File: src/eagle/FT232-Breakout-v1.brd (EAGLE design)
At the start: 37.8 x 38.1 mm, 19 parts, among them T1 BC547, U1 FT232RL-BASICSSOP

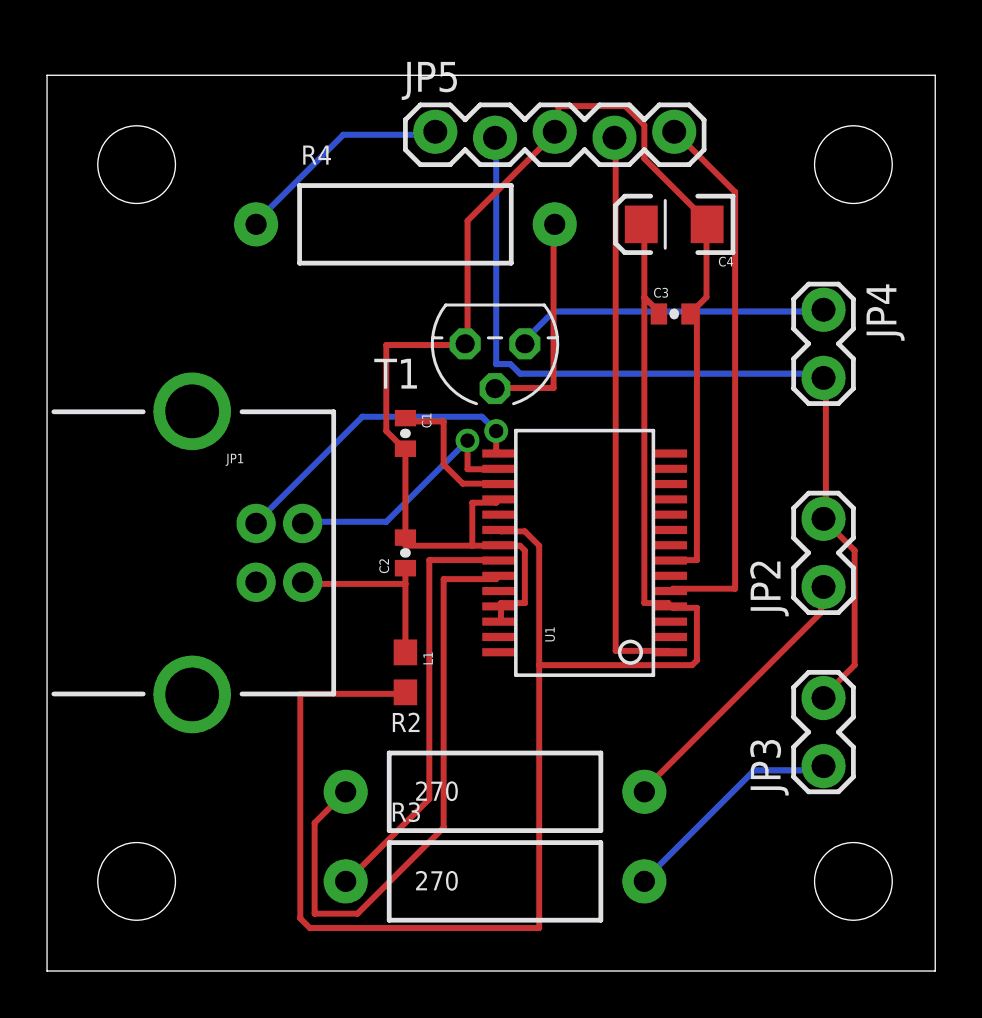
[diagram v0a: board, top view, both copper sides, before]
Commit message: modified daughter board for production
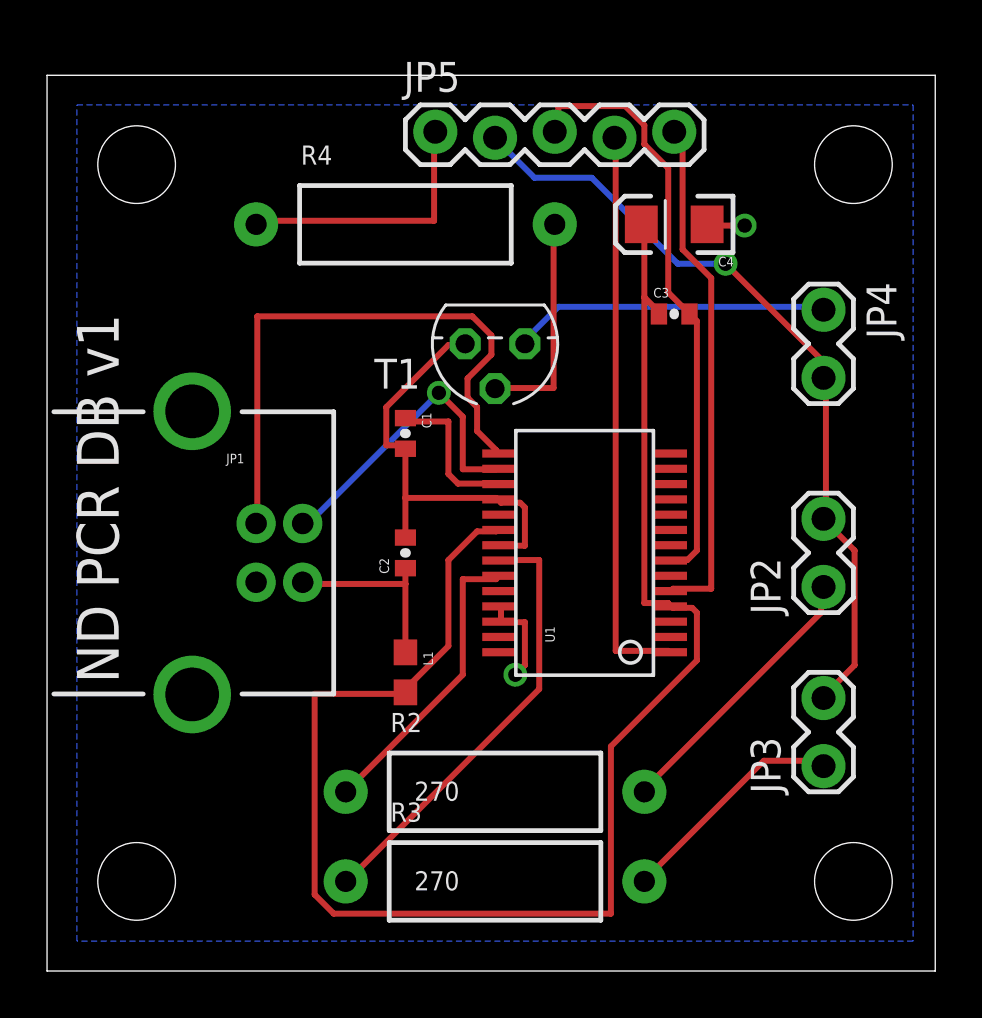
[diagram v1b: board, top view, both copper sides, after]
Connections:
- net GND: now also JP1.GND
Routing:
- net N$8: track 25.7 -> 12.7 mm
- net GND: track 62.3 -> 50.2 mm, vias 0 -> 2
- net N$5: track 13.3 -> 25.1 mm, vias 1 -> 0
- net VCC: track 38.6 -> 33.4 mm, vias 0 -> 1
- net V5: track 71.2 -> 68.3 mm
- net N$4: track 11.0 -> 13.3 mm
- net BUZZIN: track 9.33 -> 11.5 mm
- net RX: track 23.3 -> 21.9 mm
- net N$7: track 18.1 -> 18.8 mm
- added copper zone on layer 16, net GND
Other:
- board text added: "ND PCR DB v1"
